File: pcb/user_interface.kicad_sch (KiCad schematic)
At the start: 20 parts, among them Q6 NTR4003N, SW4 GSPTS0018, SW5 GSPTS0018, SW6 GSPTS0018, SW7 GSPTS0018

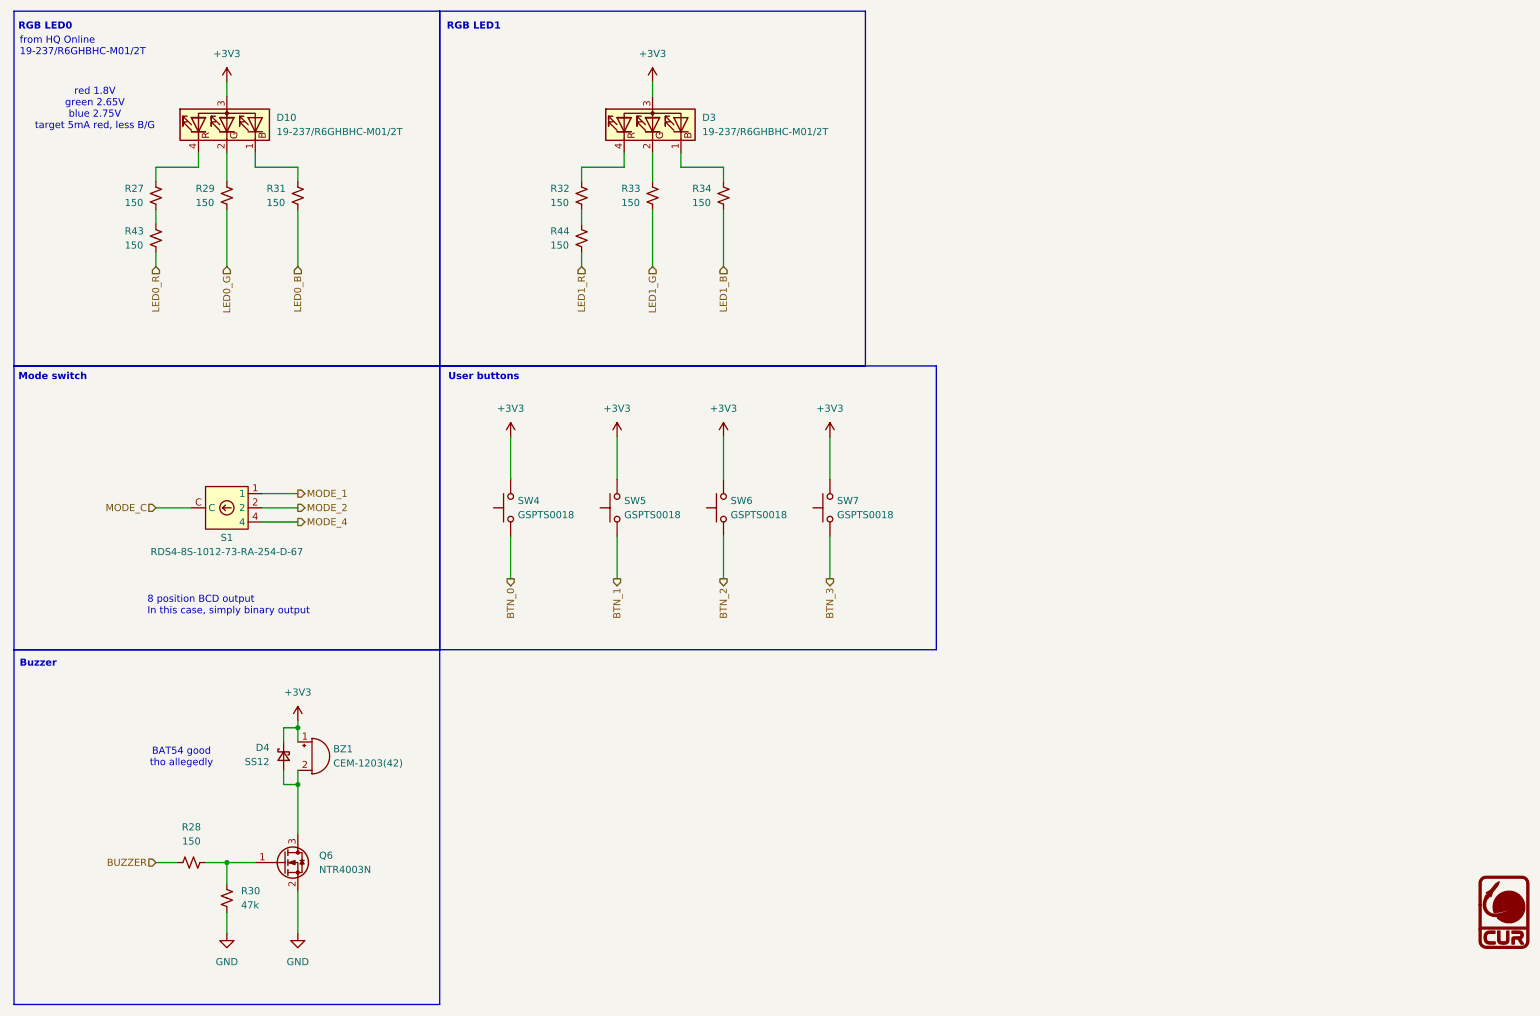
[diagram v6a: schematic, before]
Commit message: Redo layout and routing for RGB LEDs
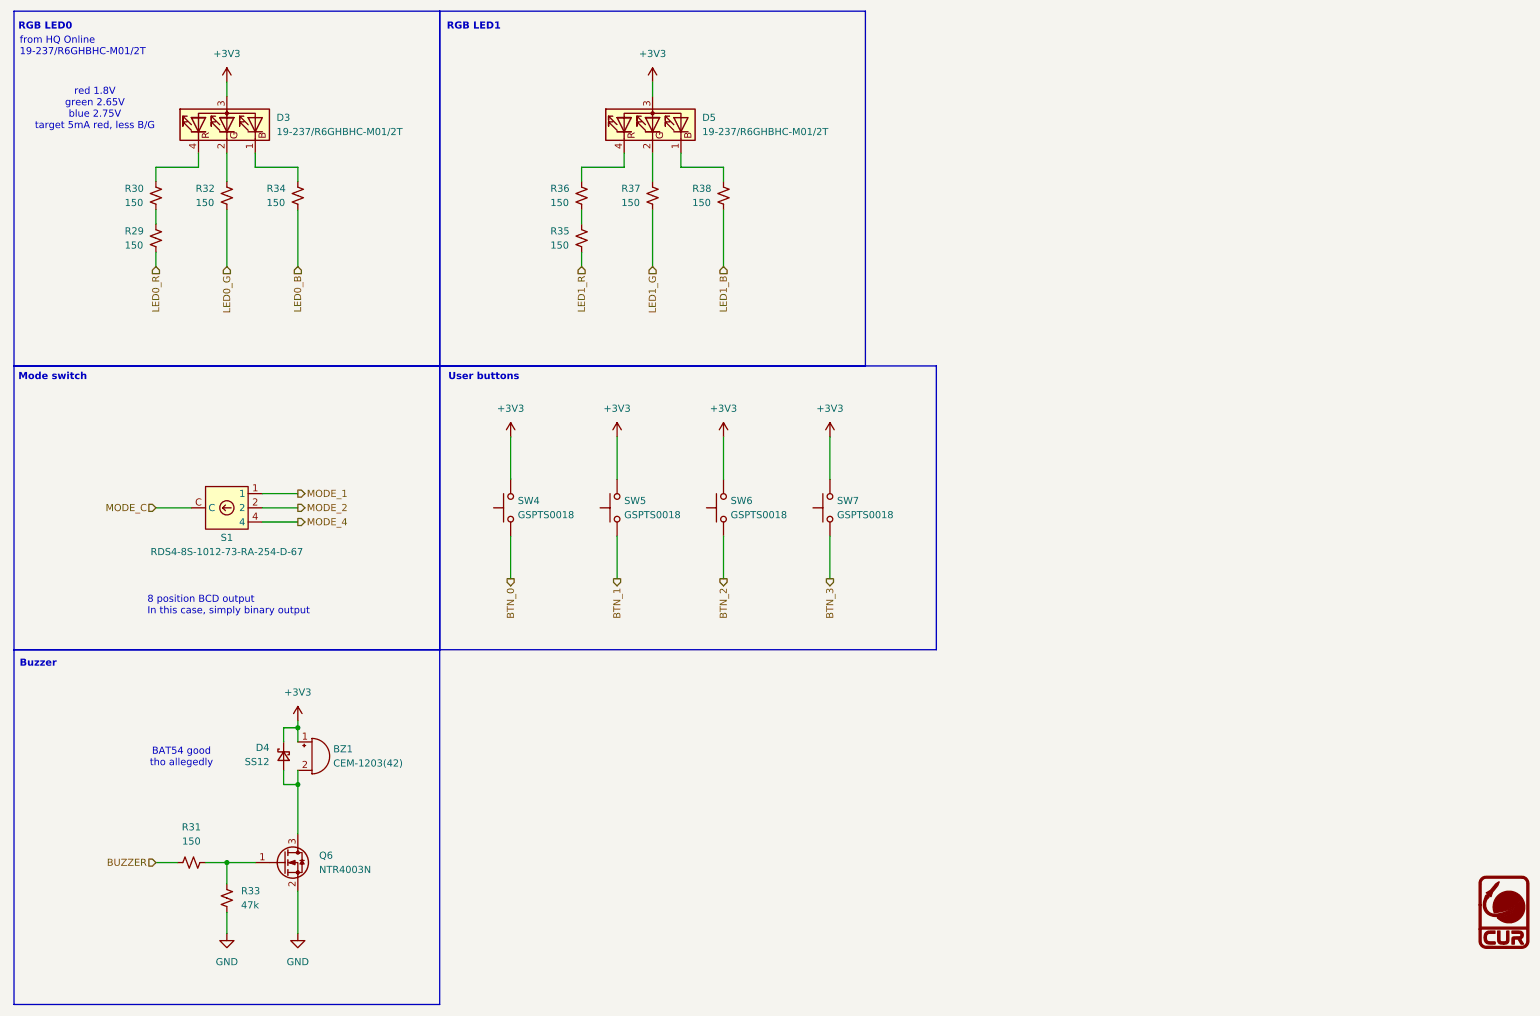
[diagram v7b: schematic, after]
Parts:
- renumbered D10 to D3, D3 to D5, R27 to R29, R43 to R30, R28 to R31, R29 to R32, R30 to R33, R31 to R34, R32 to R35, R44 to R36, R33 to R37, R34 to R38
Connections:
- net LED0_R: now also R29.2; no longer R30.2
- net LED1_R: now also R35.2; no longer R36.2
- net at D3.4 (RK): now also R30.1; no longer R29.1
- net at R35.1: now also R36.2; no longer D5.4 (RK)
- net at R36.1: now also D5.4 (RK); no longer R35.2
- new net: R29.1, R30.2
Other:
- moved on the sheet: R29, R30, R35, R36

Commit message: Reannotate and run DRC
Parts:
- renumbered R30 to R29, R29 to R30, R36 to R35, R35 to R36
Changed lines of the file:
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@@
 		(on_board yes)
 		(dnp no)
-		(property "Reference" "R35"
+		(property "Reference" "R36"
 			(at 108.712 52.07 0)
 			(effects
@@
 			(project "airbrake_mod"
 				(path "/1f4fd4ed-9886-4375-a5ac-dc32d5760936/0a32b07f-7988-40ae-8006-b298a5ae2a50"
-					(reference "R35")
+					(reference "R36")
 					(unit 1)
 				)
@@
 		(on_board yes)
 		(dnp no)
-		(property "Reference" "R36"
+		(property "Reference" "R35"
 			(at 108.712 44.45 0)
 			(effects
@@
 			(project "airbrake_mod"
 				(path "/1f4fd4ed-9886-4375-a5ac-dc32d5760936/0a32b07f-7988-40ae-8006-b298a5ae2a50"
-					(reference "R36")
+					(reference "R35")
 					(unit 1)
 				)
@@
 		(on_board yes)
 		(dnp no)
-		(property "Reference" "R29"
+		(property "Reference" "R30"
 			(at 32.512 52.07 0)
 			(effects
@@
 			(project "airbrake_mod"
 				(path "/1f4fd4ed-9886-4375-a5ac-dc32d5760936/0a32b07f-7988-40ae-8006-b298a5ae2a50"
-					(reference "R29")
+					(reference "R30")
 					(unit 1)
 				)
@@
 		(on_board yes)
 		(dnp no)
-		(property "Reference" "R30"
+		(property "Reference" "R29"
 			(at 32.512 44.45 0)
 			(effects
@@
 			(project "airbrake_mod"
 				(path "/1f4fd4ed-9886-4375-a5ac-dc32d5760936/0a32b07f-7988-40ae-8006-b298a5ae2a50"
-					(reference "R30")
-					(unit 1)
-				)
+					(reference "R29")
+					(unit 1)
+				)
